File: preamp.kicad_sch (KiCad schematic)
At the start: 8 parts, among them U4 LMV321LILT

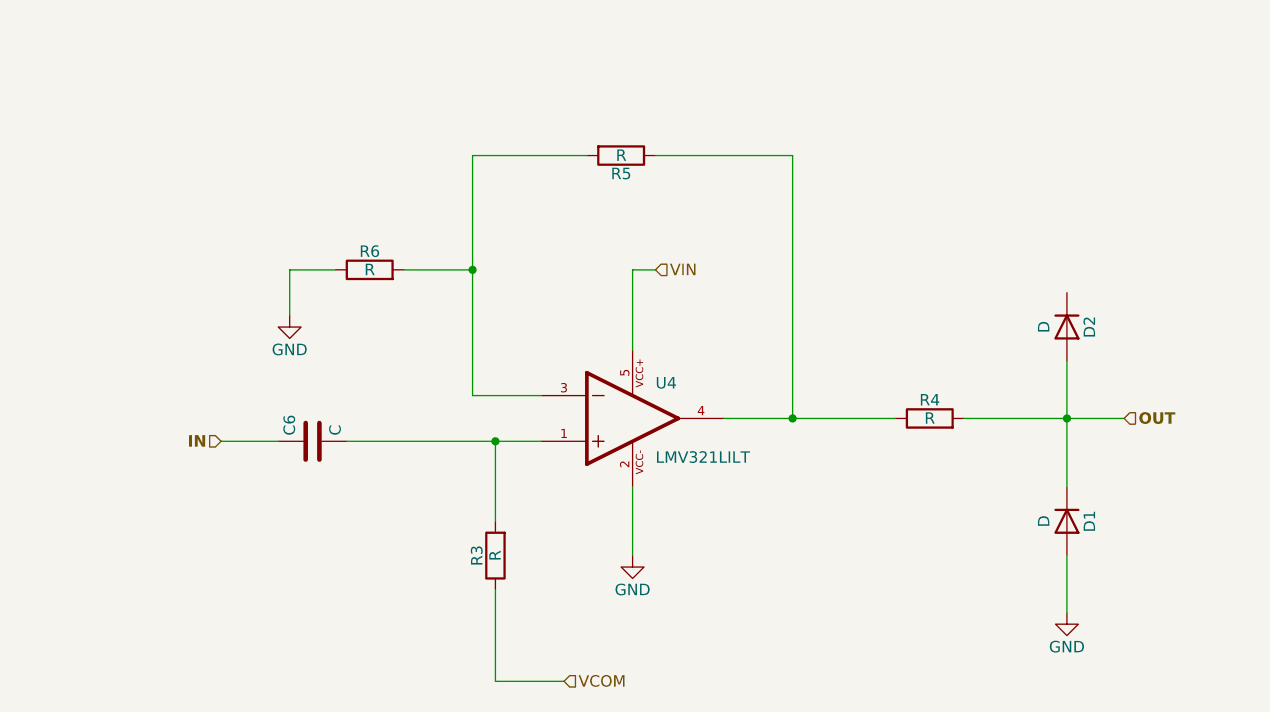
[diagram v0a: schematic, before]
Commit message: Add oscillator, mounting holes, switches
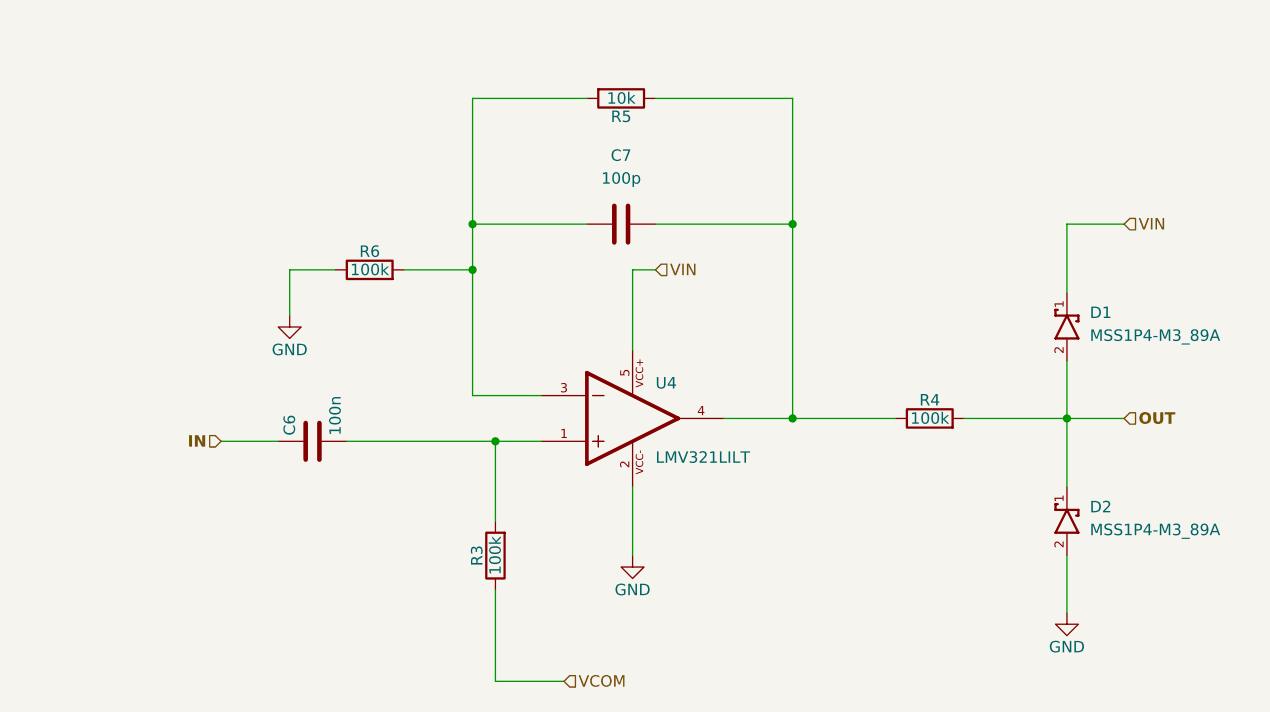
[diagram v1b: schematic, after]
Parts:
- removed D1, D2: D, symbol Device:D
- added C7: 100p, Capacitor_SMD:C_0201_0603Metric_Pad0.64x0.40mm_HandSolder, symbol Device:C
- added D1, D2: MSS1P4-M3_89A, Project_Components:MSS1P4-M3_89A, symbol Project_Components:MSS1P4-M3_89A
- C6: value C -> 100n; footprint (none) -> Capacitor_SMD:C_0201_0603Metric_Pad0.64x0.40mm_HandSolder
- R3, R4, R6: value R -> 100k; footprint (none) -> Resistor_SMD:R_0603_1608Metric_Pad0.98x0.95mm_HandSolder
- R5: value R -> 10k; footprint (none) -> Resistor_SMD:R_0603_1608Metric_Pad0.98x0.95mm_HandSolder
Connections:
- net GND: now also D2.2
- net OUT: now also D1.2, D2.1
- net VIN: now also D1.1
- net at R4.1, R5.1, U4.4: now also C7.1
- net at R5.2, R6.2, U4.3: now also C7.2
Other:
- moved on the sheet: R5

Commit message: Complete pre-amp and pre-amp sim
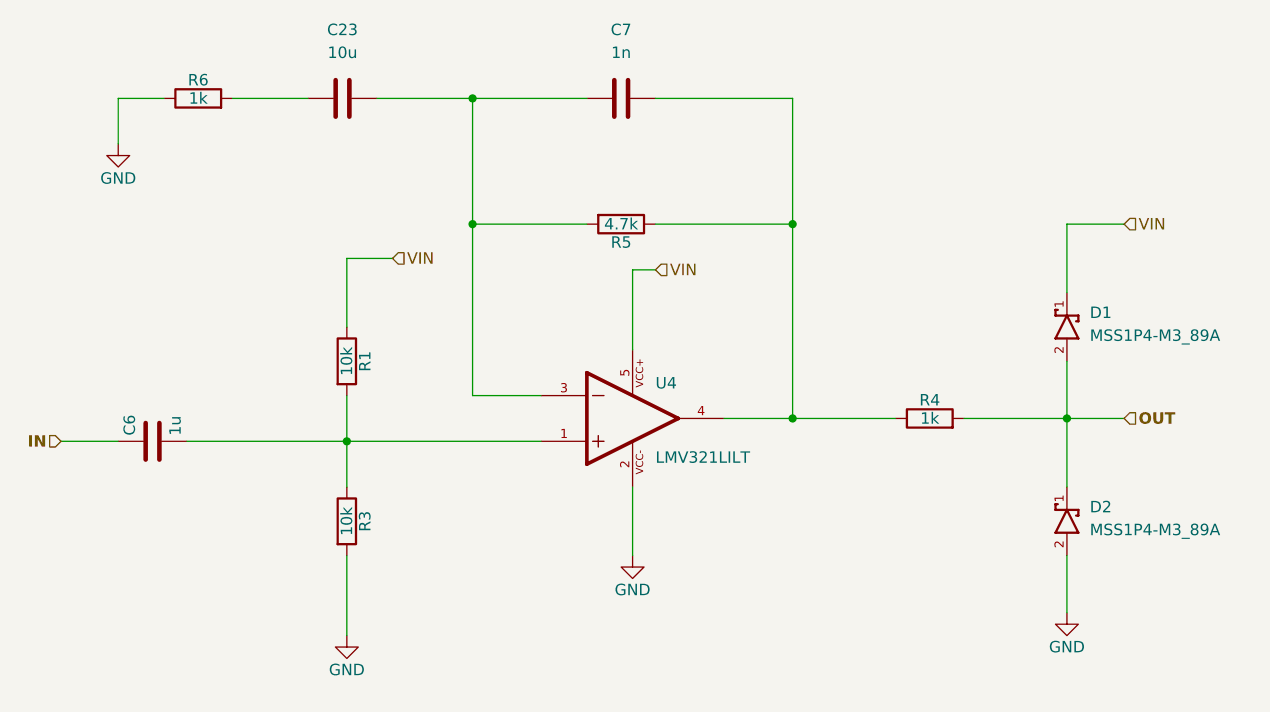
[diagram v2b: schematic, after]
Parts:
- added C23: 10u, Capacitor_SMD:C_0201_0603Metric_Pad0.64x0.40mm_HandSolder, symbol Device:C
- added R1: 10k, Resistor_SMD:R_0603_1608Metric_Pad0.98x0.95mm_HandSolder, symbol Device:R
- C6: value 100n -> 1u
- C7: value 100p -> 1n
- R3: value 100k -> 10k
- R4, R6: value 100k -> 1k
- R5: value 10k -> 4.7k
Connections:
- net VCOM is gone; now on an unnamed net: R3.1
- net GND: now also R3.2
- net VIN: now also R1.1
- net at C6.2, U4.1: now also R1.2; no longer R3.2
- net at C7.2, R5.2, U4.3: now also C23.1; no longer R6.2
- new net: C23.2, R6.2
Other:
- moved on the sheet: C6, C7, R5, R6

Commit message: Began board layout
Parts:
- C11: renamed from C6; footprint Capacitor_SMD:C_0201_0603Metric_Pad0.64x0.40mm_HandSolder -> Capacitor_SMD:C_0603_1608Metric_Pad1.08x0.95mm_HandSolder
- C12: renamed from C23; footprint Capacitor_SMD:C_0201_0603Metric_Pad0.64x0.40mm_HandSolder -> Capacitor_SMD:C_0603_1608Metric_Pad1.08x0.95mm_HandSolder
- C13: renamed from C7; footprint Capacitor_SMD:C_0201_0603Metric_Pad0.64x0.40mm_HandSolder -> Capacitor_SMD:C_0603_1608Metric_Pad1.08x0.95mm_HandSolder
- renumbered D1 to D2, D2 to D3, R6 to R10, R1 to R11, R3 to R12, R5 to R13, R4 to R14, U4 to U3
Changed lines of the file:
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@@
+	(wire
+		(pts
+			(xy 109.22 92.71) (xy 109.22 97.79)
+		)
+		(stroke
+			(width 0)
+			(type default)
+		)
+	)
+	(wire
+		(pts
+			(xy 158.75 90.17) (xy 151.13 90.17)
+		)
+		(stroke
+			(width 0)
+			(type default)
+		)
+	)
+	(wire
+		(pts
+			(xy 189.23 90.17) (xy 195.58 90.17)
+		)
+		(stroke
+			(width 0)
+			(type default)
+		)
+	)
 	(wire
 		(pts
 			(xy 96.52 54.61) (xy 104.929 54.61)
-		)
-		(stroke
-			(width 0)
-			(type default)
-		)
-	)
-	(wire
-		(pts
-			(xy 109.22 92.71) (xy 109.22 97.79)
-		)
-		(stroke
-			(width 0)
-			(type default)
-		)
-	)
-	(wire
-		(pts
-			(xy 158.75 90.17) (xy 151.13 90.17)
-		)
-		(stroke
-			(width 0)
-			(type default)
-		)
-	)
-	(wire
-		(pts
-			(xy 189.23 90.17) (xy 195.58 90.17)
 		)
 		(stroke
@@
 		(on_board yes)
 		(dnp no)
-		(property "Reference" "#PWR06"
+		(property "Reference" "#PWR028"
 			(at 189.23 118.11 0)
 			(effects
@@
 			(project "pitch shifter"
 				(path "/155ecfb0-8543-4b20-91a8-ba83977b0554/383a7b3f-5ddf-4f9a-8e46-e2c3d50c1497"
-					(reference "#PWR06")
+					(reference "#PWR028")
 					(unit 1)
 				)
@@
 		(on_board yes)
 		(dnp no)
-		(property "Reference" "#PWR08"
+		(property "Reference" "#PWR027"
 			(at 140.97 111.76 0)
 			(effects
@@
 			(project "pitch shifter"
 				(path "/155ecfb0-8543-4b20-91a8-ba83977b0554/383a7b3f-5ddf-4f9a-8e46-e2c3d50c1497"
-					(reference "#PWR08")
+					(reference "#PWR027")
 					(unit 1)
 				)
@@
 		(on_board yes)
 		(dnp no)
-		(property "Reference" "R1"
+		(property "Reference" "R11"
 			(at 111.252 83.82 90)
 			(effects
@@
 			(project "pitch shifter"
 				(path "/155ecfb0-8543-4b20-91a8-ba83977b0554/383a7b3f-5ddf-4f9a-8e46-e2c3d50c1497"
-					(reference "R1")
+					(reference "R11")
 					(unit 1)
 				)
@@
 		(on_board yes)
 		(dnp no)
-		(property "Reference" "#PWR028"
+		(property "Reference" "#PWR026"
 			(at 109.22 120.65 0)
 			(effects
@@
 			(project "pitch shifter"
 				(path "/155ecfb0-8543-4b20-91a8-ba83977b0554/383a7b3f-5ddf-4f9a-8e46-e2c3d50c1497"
-					(reference "#PWR028")
+					(reference "#PWR026")
 					(unit 1)
 				)
@@
 		(on_board yes)
 		(dnp no)
-		(property "Reference" "R4"
+		(property "Reference" "R14"
 			(at 173.99 88.138 90)
 			(effects
@@
 			(project "pitch shifter"
 				(path "/155ecfb0-8543-4b20-91a8-ba83977b0554/383a7b3f-5ddf-4f9a-8e46-e2c3d50c1497"
-					(reference "R4")
+					(reference "R14")
 					(unit 1)
 				)
@@
 		(on_board yes)
 		(dnp no)
-		(property "Reference" "C6"
+		(property "Reference" "C11"
 			(at 85.09 92.075 0)
 			(effects
@@
 			)
 		)
-		(property "Footprint" "Capacitor_SMD:C_0201_0603Metric_Pad0.64x0.40mm_HandSolder"
+		(property "Footprint" "Capacitor_SMD:C_0603_1608Metric_Pad1.08x0.95mm_HandSolder"
 			(at 91.44 91.7448 0)
 			(effects
@@
 			(project ""
 				(path "/155ecfb0-8543-4b20-91a8-ba83977b0554/383a7b3f-5ddf-4f9a-8e46-e2c3d50c1497"
-					(reference "C6")
+					(reference "C11")
 					(unit 1)
 				)
@@
 		(dnp no)
 		(fields_autoplaced yes)
-		(property "Reference" "D2"
+		(property "Reference" "D3"
 			(at 191.77 100.0124 90)
 			(effects
@@
 			(project "pitch shifter"
 				(path "/155ecfb0-8543-4b20-91a8-ba83977b0554/383a7b3f-5ddf-4f9a-8e46-e2c3d50c1497"
-					(reference "D2")
+					(reference "D3")
 					(unit 1)
 				)
@@
 		(on_board yes)
 		(dnp no)
-		(property "Reference" "R6"
+		(property "Reference" "R10"
 			(at 92.71 52.578 90)
 			(effects
@@
 			(project "pitch shifter"
 				(path "/155ecfb0-8543-4b20-91a8-ba83977b0554/383a7b3f-5ddf-4f9a-8e46-e2c3d50c1497"
-					(reference "R6")
+					(reference "R10")
 					(unit 1)
 				)
@@
 		(on_board yes)
 		(dnp no)
-		(property "Reference" "U4"
+		(property "Reference" "U3"
 			(at 143.51 86.995 0)
 			(effects
@@
 			(project ""
 				(path "/155ecfb0-8543-4b20-91a8-ba83977b0554/383a7b3f-5ddf-4f9a-8e46-e2c3d50c1497"
-					(reference "U4")
+					(reference "U3")
 					(unit 1)
 				)
@@
 		(on_board yes)
 		(dnp no)
-		(property "Reference" "C23"
+		(property "Reference" "C12"
 			(at 108.739 46.99 90)
 			(effects
@@
 			)
 		)
-		(property "Footprint" "Capacitor_SMD:C_0201_0603Metric_Pad0.64x0.40mm_HandSolder"
+		(property "Footprint" "Capacitor_SMD:C_0603_1608Metric_Pad1.08x0.95mm_HandSolder"
 			(at 104.929 55.5752 0)
 			(effects
@@
 			(project "pitch shifter"
 				(path "/155ecfb0-8543-4b20-91a8-ba83977b0554/383a7b3f-5ddf-4f9a-8e46-e2c3d50c1497"
-					(reference "C23")
+					(reference "C12")
 					(unit 1)
 				)
@@
 		(on_board yes)
 		(dnp no)
-		(property "Reference" "R3"
+		(property "Reference" "R12"
 			(at 111.252 101.6 90)
 			(effects
@@
 			(project "pitch shifter"
 				(path "/155ecfb0-8543-4b20-91a8-ba83977b0554/383a7b3f-5ddf-4f9a-8e46-e2c3d50c1497"
-					(reference "R3")
+					(reference "R12")
 					(unit 1)
 				)
@@
 		(on_board yes)
 		(dnp no)
-		(property "Reference" "#PWR07"
+		(property "Reference" "#PWR025"
 			(at 83.82 66.04 0)
 			(effects
@@
 			(project "pitch shifter"
 				(path "/155ecfb0-8543-4b20-91a8-ba83977b0554/383a7b3f-5ddf-4f9a-8e46-e2c3d50c1497"
-					(reference "#PWR07")
+					(reference "#PWR025")
 					(unit 1)
 				)
@@
 		(on_board yes)
 		(dnp no)
-		(property "Reference" "R5"
+		(property "Reference" "R13"
 			(at 139.7 70.612 90)
 			(effects
@@
 			(project "pitch shifter"
 				(path "/155ecfb0-8543-4b20-91a8-ba83977b0554/383a7b3f-5ddf-4f9a-8e46-e2c3d50c1497"
-					(reference "R5")
+					(reference "R13")
 					(unit 1)
 				)
@@
 		(dnp no)
 		(fields_autoplaced yes)
-		(property "Reference" "D1"
+		(property "Reference" "D2"
 			(at 191.77 78.4224 90)
 			(effects
@@
 			(project ""
 				(path "/155ecfb0-8543-4b20-91a8-ba83977b0554/383a7b3f-5ddf-4f9a-8e46-e2c3d50c1497"
-					(reference "D1")
+					(reference "D2")
 					(unit 1)
 				)
@@
 		(on_board yes)
 		(dnp no)
-		(property "Reference" "C7"
+		(property "Reference" "C13"
 			(at 139.7 46.99 90)
 			(effects
@@
 			)
 		)
-		(property "Footprint" "Capacitor_SMD:C_0201_0603Metric_Pad0.64x0.40mm_HandSolder"
+		(property "Footprint" "Capacitor_SMD:C_0603_1608Metric_Pad1.08x0.95mm_HandSolder"
 			(at 135.89 55.5752 0)
 			(effects
@@
 			(project ""
 				(path "/155ecfb0-8543-4b20-91a8-ba83977b0554/383a7b3f-5ddf-4f9a-8e46-e2c3d50c1497"
-					(reference "C7")
+					(reference "C13")
 					(unit 1)
 				)
